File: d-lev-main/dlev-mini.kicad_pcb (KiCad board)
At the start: 4 copper layers, 175.3 x 163.3 mm, 114 parts, among them J1 Conn_01x12_MountingPin, J2 Tag-Connect TC2030-NL, J3 S8B-PH-SM4-TB, J4 S8B-PH-SM4-TB, J5 Conn_01x06_MountingPin, Q1 BSS138, Q3 BSS138, Q4 BSS138, Q5 BSS138, SW1 RotaryEncoder_Switch, SW2 RotaryEncoder_Switch, SW3 RotaryEncoder_Switch, SW4 RotaryEncoder_Switch, SW5 RotaryEncoder_Switch, SW6 RotaryEncoder_Switch, SW7 RotaryEncoder_Switch, SW8 RotaryEncoder_Switch, U1 25LCxxx, U2 AMS1117-3.3, U3 AC608

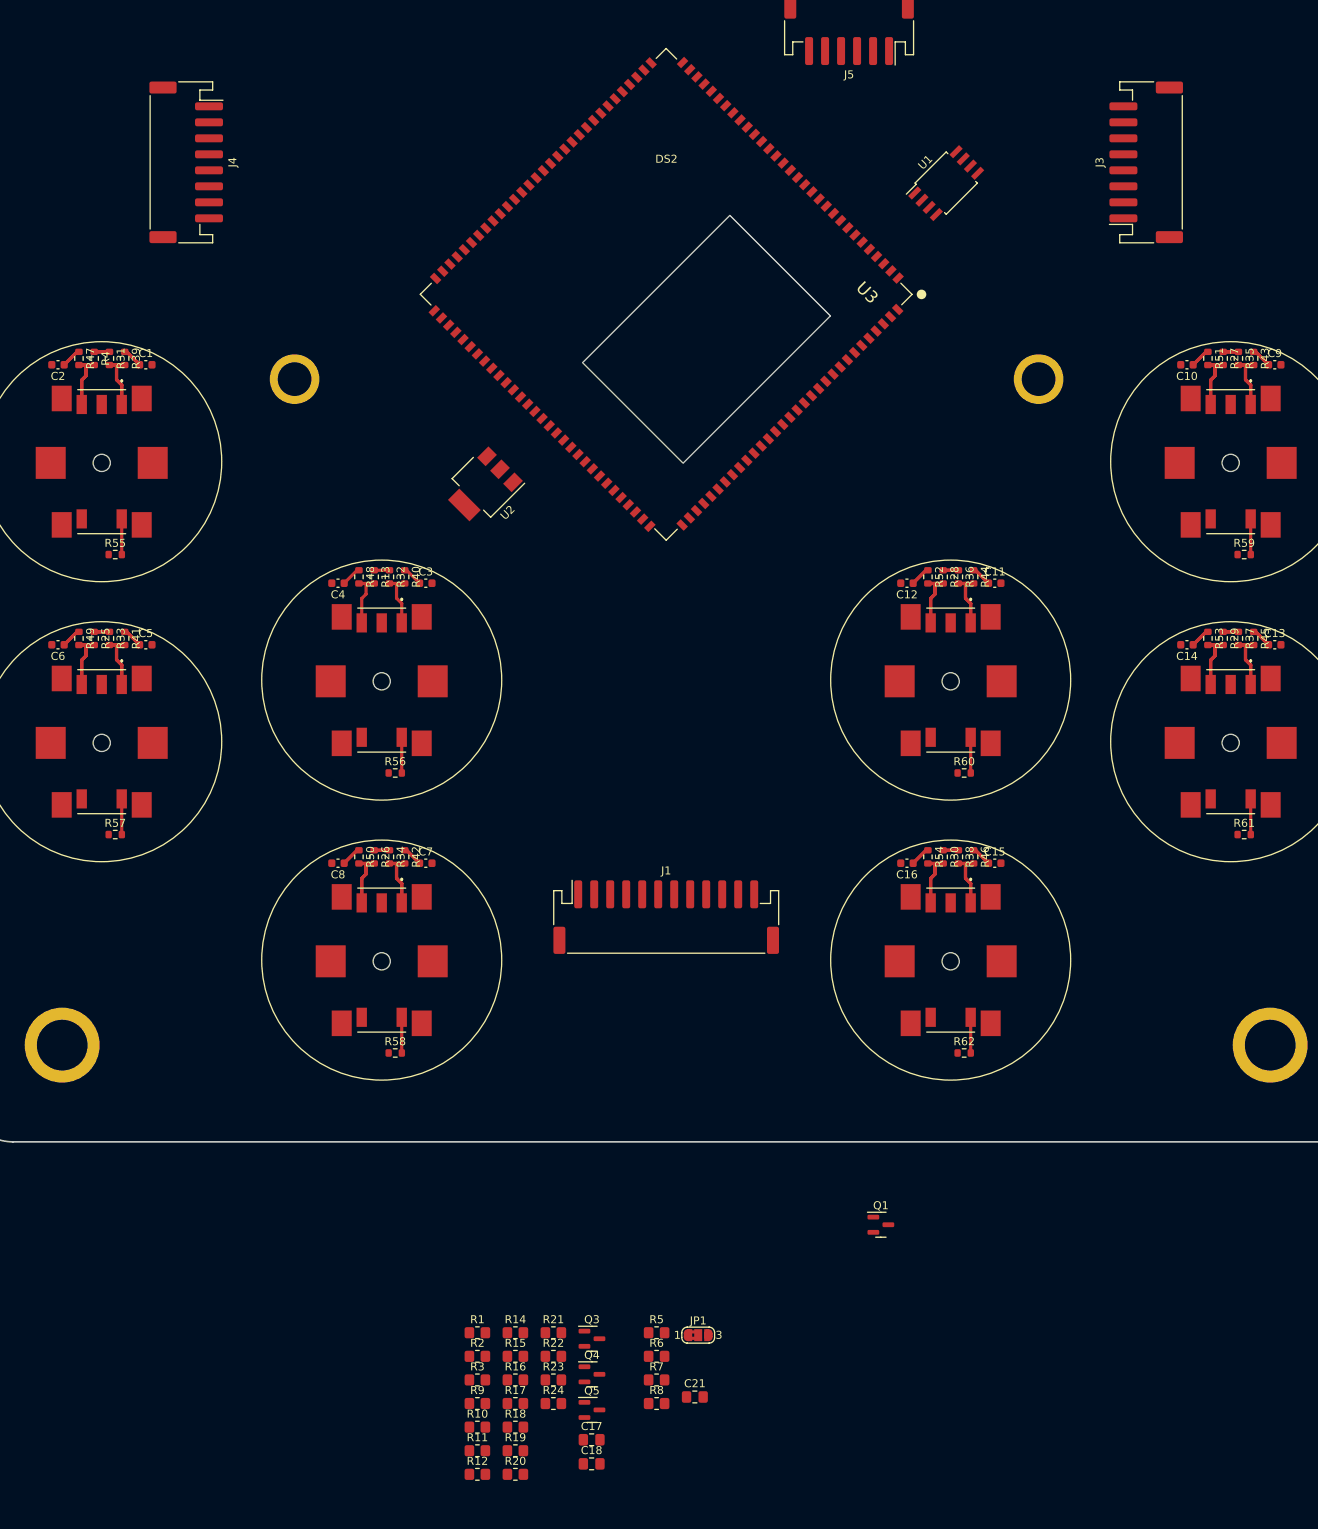
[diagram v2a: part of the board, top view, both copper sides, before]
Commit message: Pinned out FPGA and rearranged encoders again
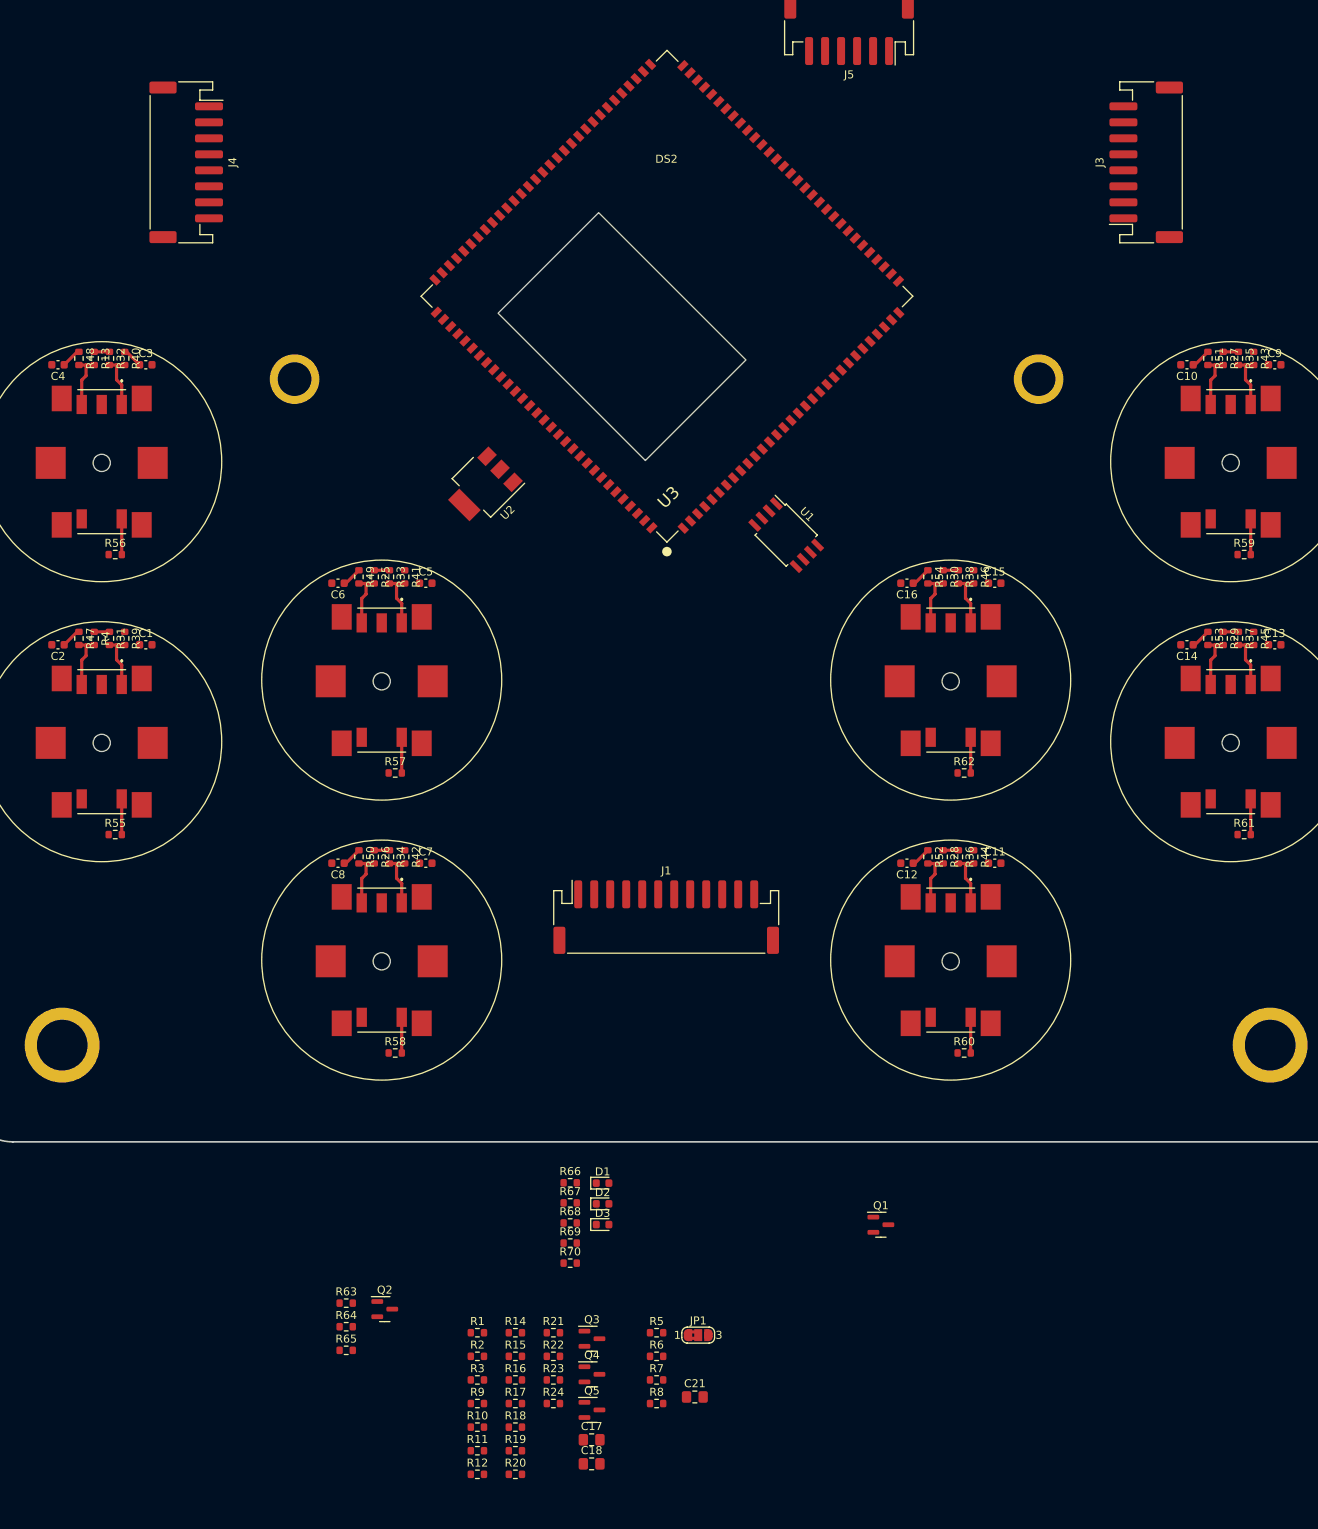
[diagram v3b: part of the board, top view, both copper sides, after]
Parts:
- added D1: LED, LED_SMD:LED_0603_1608Metric, F.Cu at (-7.95, 58.0)
- added D2: LED, LED_SMD:LED_0603_1608Metric, F.Cu at (-7.95, 60.6)
- added D3: LED, LED_SMD:LED_0603_1608Metric, F.Cu at (-7.95, 63.2)
- added Q2: BSS138, Package_TO_SOT_SMD:SOT-23, F.Cu at (-35.2, 73.8)
- added R63: 10k, Resistor_SMD:R_0603_1608Metric, F.Cu at (-40.0, 73.0)
- added R64: 10k, Resistor_SMD:R_0603_1608Metric, F.Cu at (-40.0, 76.0)
- added R65: 220, Resistor_SMD:R_0603_1608Metric, F.Cu at (-40.0, 78.9)
- added R66: 1k, Resistor_SMD:R_0603_1608Metric, F.Cu at (-12.0, 58.0)
- added R67: 1k, Resistor_SMD:R_0603_1608Metric, F.Cu at (-12.0, 60.5)
- added R68: 1k, Resistor_SMD:R_0603_1608Metric, F.Cu at (-12.0, 63.0)
- added R69: 10k, Resistor_SMD:R_0603_1608Metric, F.Cu at (-12.0, 65.5)
- added R70: 10k, Resistor_SMD:R_0603_1608Metric, F.Cu at (-12.0, 68.0)
- R1, R10, R11, R12, R14, R15, R16, R17, R18, R19, R2, R20, R21, R22, R23, R24, R3, R5, R6, R7, R8, R9: footprint Resistor_SMD:R_0805_2012Metric_Pad1.20x1.40mm_HandSolder -> Resistor_SMD:R_0603_1608Metric
- R13, R25, R26, R27, R28, R29, R30, R31, R32, R33, R34, R35, R36, R37, R38, R39, R4, R40, R41, R42, R43, R44, R45, R46, R47, R48, R49, R50, R51, R52, R53, R54, R55, R56, R57, R58, R59, R60, R61, R62: value R_Small -> 10k
- moved U1 48.3 mm to (15.0, -23.0), turned to -45 degrees
- moved C4 44.4 mm to (-76.0, -44.3)
- moved R13 44.4 mm to (-71.5, -45.1)
- moved R32 44.4 mm to (-69.6, -45.1)
- moved R48 44.4 mm to (-73.4, -45.1)
- moved R56 44.4 mm to (-68.9, -20.6)
- moved C3 44.4 mm to (-65.1, -44.3)
- moved R40 44.4 mm to (-67.7, -45.1)
- moved U3 43.2 mm to (-30.6, -52.9), turned to -45 degrees
- moved C6 35.8 mm to (-41.0, -17.0)
- moved R25 35.8 mm to (-36.5, -17.8)
- moved R33 35.8 mm to (-34.6, -17.8)
- moved R49 35.8 mm to (-38.4, -17.8)
- moved R57 35.8 mm to (-33.9, 6.73)
- moved C5 35.8 mm to (-30.1, -17.0)
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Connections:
- C1 pad 1: enc_2.a -> /FPGA/enc_2.b
- C10 pad 1: enc_6.b -> /FPGA/enc_5.a
- C11 pad 1: enc_5.a -> /FPGA/enc_8.b
- C12 pad 1: enc_5.b -> /FPGA/enc_8.a
- C13 pad 1: enc_7.a -> /FPGA/enc_6.b
- C14 pad 1: enc_7.b -> /FPGA/enc_6.a
- C15 pad 1: enc_8.a -> /FPGA/enc_7.b
- C16 pad 1: enc_8.b -> /FPGA/enc_7.a
- C2 pad 1: enc_2.b -> /FPGA/enc_2.a
- C3 pad 1: enc_1.a -> /FPGA/enc_1.b
- C4 pad 1: enc_1.b -> /FPGA/enc_1.a
- C5 pad 1: enc_3.a -> /FPGA/enc_3.b
- C6 pad 1: enc_3.b -> /FPGA/enc_3.a
- C7 pad 1: enc_4.a -> /FPGA/enc_4.b
- C8 pad 1: enc_4.b -> /FPGA/enc_4.a
- C9 pad 1: enc_6.a -> /FPGA/enc_5.b
- J1 pad 3: uart_tx_5v -> midi_out_lo
- J1 pad 4: uart_rx_5v -> midi_in
- J1 pad 5: midi_out_lo -> uart_tx_5v
- J1 pad 6: midi_in -> uart_rx_5v
- R13 pad 2: /encoder/B1 -> /encoder/A1
- R25 pad 2: /encoder2/B1 -> /encoder2/A1
- R26 pad 2: /encoder3/B1 -> /encoder3/A1
- R27 pad 2: /encoder4/B1 -> /encoder4/A1
- R28 pad 2: /encoder7/B1 -> /encoder7/A1
- R29 pad 2: /encoder5/B1 -> /encoder5/A1
- R30 pad 2: /encoder6/B1 -> /encoder6/A1
- R31 pad 2: /encoder1/A1 -> /encoder1/B1
- R32 pad 2: /encoder/A1 -> /encoder/B1
- R33 pad 2: /encoder2/A1 -> /encoder2/B1
- R34 pad 2: /encoder3/A1 -> /encoder3/B1
- R35 pad 2: /encoder4/A1 -> /encoder4/B1
- R36 pad 2: /encoder7/A1 -> /encoder7/B1
- R37 pad 2: /encoder5/A1 -> /encoder5/B1
- R38 pad 2: /encoder6/A1 -> /encoder6/B1
- R39 pad 1: enc_2.a -> /FPGA/enc_2.b
- R39 pad 2: /encoder1/A1 -> /encoder1/B1
- R4 pad 2: /encoder1/B1 -> /encoder1/A1
- R40 pad 1: enc_1.a -> /FPGA/enc_1.b
- R40 pad 2: /encoder/A1 -> /encoder/B1
- R41 pad 1: enc_3.a -> /FPGA/enc_3.b
- R41 pad 2: /encoder2/A1 -> /encoder2/B1
- R42 pad 1: enc_4.a -> /FPGA/enc_4.b
- R42 pad 2: /encoder3/A1 -> /encoder3/B1
- R43 pad 1: enc_6.a -> /FPGA/enc_5.b
- R43 pad 2: /encoder4/A1 -> /encoder4/B1
- R44 pad 1: enc_5.a -> /FPGA/enc_8.b
- R44 pad 2: /encoder7/A1 -> /encoder7/B1
- R45 pad 1: enc_7.a -> /FPGA/enc_6.b
- R45 pad 2: /encoder5/A1 -> /encoder5/B1
- R46 pad 1: enc_8.a -> /FPGA/enc_7.b
- R46 pad 2: /encoder6/A1 -> /encoder6/B1
- R47 pad 1: enc_2.b -> /FPGA/enc_2.a
- R47 pad 2: /encoder1/B1 -> /encoder1/A1
- R48 pad 1: enc_1.b -> /FPGA/enc_1.a
- R48 pad 2: /encoder/B1 -> /encoder/A1
- R49 pad 1: enc_3.b -> /FPGA/enc_3.a
- R49 pad 2: /encoder2/B1 -> /encoder2/A1
- R50 pad 1: enc_4.b -> /FPGA/enc_4.a
- R50 pad 2: /encoder3/B1 -> /encoder3/A1
- R51 pad 1: enc_6.b -> /FPGA/enc_5.a
- R51 pad 2: /encoder4/B1 -> /encoder4/A1
- R52 pad 1: enc_5.b -> /FPGA/enc_8.a
- R52 pad 2: /encoder7/B1 -> /encoder7/A1
- R53 pad 1: enc_7.b -> /FPGA/enc_6.a
- R53 pad 2: /encoder5/B1 -> /encoder5/A1
- R54 pad 1: enc_8.b -> /FPGA/enc_7.a
- R54 pad 2: /encoder6/B1 -> /encoder6/A1
- R55 pad 2: enc_2.s -> /FPGA/enc_2.s
- R56 pad 2: enc_1.s -> /FPGA/enc_1.s
- R57 pad 2: enc_3.s -> /FPGA/enc_3.s
- R58 pad 2: enc_4.s -> /FPGA/enc_4.s
- R59 pad 2: enc_6.s -> /FPGA/enc_5.s
- R60 pad 2: enc_5.s -> /FPGA/enc_8.s
- R61 pad 2: enc_7.s -> /FPGA/enc_6.s
- R62 pad 2: enc_8.s -> /FPGA/enc_7.s
- SW1 pad S1: enc_2.s -> /FPGA/enc_2.s
- SW2 pad S1: enc_1.s -> /FPGA/enc_1.s
- SW3 pad S1: enc_3.s -> /FPGA/enc_3.s
- SW4 pad S1: enc_4.s -> /FPGA/enc_4.s
- SW5 pad S1: enc_6.s -> /FPGA/enc_5.s
- SW6 pad S1: enc_5.s -> /FPGA/enc_8.s
- SW7 pad S1: enc_7.s -> /FPGA/enc_6.s
- SW8 pad S1: enc_8.s -> /FPGA/enc_7.s
- U3 pad 1: unconnected-(U3-IO_T14-Pad1) -> /spdif_tx_0
- U3 pad 10: unconnected-(U3-IO_L15-Pad10) -> /FPGA/mem_spi.di
- U3 pad 100: unconnected-(U3-IO_R3-Pad100) -> /FPGA/enc_3.a
- U3 pad 101: unconnected-(U3-IO_T3-Pad101) -> /FPGA/enc_3.b
- U3 pad 102: unconnected-(U3-IO_R4-Pad102) -> /FPGA/enc_3.s
- U3 pad 103: unconnected-(U3-IO_T4-Pad103) -> /FPGA/enc_4.a
- U3 pad 104: unconnected-(U3-IO_R5-Pad104) -> /FPGA/enc_4.b
- U3 pad 105: unconnected-(U3-IO_T5-Pad105) -> /FPGA/enc_4.s
- U3 pad 11: unconnected-(U3-IO_L16-Pad11) -> /FPGA/mem_spi.cl
- U3 pad 12: unconnected-(U3-IO_P11-Pad12) -> /FPGA/mem_spi.do
- U3 pad 120: unconnected-(U3-IO_R12-Pad120) -> /FPGA/midi_tx_n
- U3 pad 121: unconnected-(U3-IO_T12-Pad121) -> /FPGA/midi_tx
- U3 pad 122: unconnected-(U3-IO_R13-Pad122) -> /FPGA/midi_rx
- U3 pad 123: unconnected-(U3-IO_T13-Pad123) -> /uart_tx_3v
- U3 pad 124: unconnected-(U3-IO_R14-Pad124) -> /uart_rx_3v
- U3 pad 13: unconnected-(U3-IO_N11-Pad13) -> /FPGA/mem_spi.cs
- U3 pad 2: unconnected-(U3-IO_T15-Pad2) -> /spdif_tx_1
- U3 pad 20: unconnected-(U3-IO_K16-Pad20) -> /FPGA/enc_8.s
- U3 pad 21: unconnected-(U3-IO_J15-Pad21) -> /FPGA/enc_8.b
- U3 pad 22: unconnected-(U3-IO_J16-Pad22) -> /FPGA/enc_8.a
- U3 pad 23: unconnected-(U3-IO_L14-Pad23) -> /FPGA/enc_7.s
- U3 pad 24: unconnected-(U3-IO_J14-Pad24) -> /FPGA/enc_7.b
- U3 pad 25: unconnected-(U3-IO_K15-Pad25) -> /FPGA/enc_7.a
- U3 pad 26: unconnected-(U3-IO_F16-Pad26) -> /FPGA/enc_6.s
- U3 pad 27: unconnected-(U3-IO_G15-Pad27) -> /FPGA/enc_6.b
- U3 pad 28: unconnected-(U3-IO_F15-Pad28) -> /FPGA/enc_6.a
- U3 pad 29: unconnected-(U3-I_E16-Pad29) -> /FPGA/enc_5.s
- U3 pad 3: unconnected-(U3-IO_R16-Pad3) -> acal_btn
- U3 pad 30: unconnected-(U3-IO_D16-Pad30) -> /FPGA/enc_5.b
- U3 pad 31: unconnected-(U3-IO_D15-Pad31) -> /FPGA/enc_5.a
- U3 pad 4: unconnected-(U3-IO_P15-Pad4) -> mute_btn
- U3 pad 42: unconnected-(U3-I_A9-Pad42) -> /FPGA/vol.quad
- U3 pad 44: unconnected-(U3-IO_C9-Pad44) -> /FPGA/vol.sq
- U3 pad 46: unconnected-(U3-IO_D9-Pad46) -> /FPGA/vol.zero
- U3 pad 5: unconnected-(U3-IO_P16-Pad5) -> mute_led
- U3 pad 50: unconnected-(U3-I_E1-Pad50) -> /FPGA/~{reset}
- U3 pad 53: unconnected-(U3-IO_D1-Pad53) -> /FPGA/tuner.oe
- U3 pad 54: unconnected-(U3-IO_F3-Pad54) -> /FPGA/tuner.le
- U3 pad 55: unconnected-(U3-IO_F2-Pad55) -> /FPGA/tuner.sda
- U3 pad 56: unconnected-(U3-IO_F1-Pad56) -> /FPGA/tuner.scl
- U3 pad 57: unconnected-(U3-IO_G5-Pad57) -> /FPGA/led1
- U3 pad 58: unconnected-(U3-IO_G2-Pad58) -> /FPGA/led2
- U3 pad 59: unconnected-(U3-IO_G1-Pad59) -> /FPGA/led3
- U3 pad 6: unconnected-(U3-IO_N15-Pad6) -> /FPGA/gpio_o3
- U3 pad 65: unconnected-(U3-IO_K5-Pad65) -> /FPGA/lcd_pwm
- U3 pad 66: unconnected-(U3-IO_L4-Pad66) -> /FPGA/lcd.data3
- U3 pad 67: unconnected-(U3-IO_M6-Pad67) -> /FPGA/lcd.data2
- U3 pad 68: unconnected-(U3-IO_N3-Pad68) -> /FPGA/lcd.data1
- U3 pad 69: unconnected-(U3-IO_N5-Pad69) -> /FPGA/lcd.data0
- U3 pad 7: unconnected-(U3-IO_N16-Pad7) -> /FPGA/gpio_o2
- U3 pad 70: unconnected-(U3-IO_P3-Pad70) -> /FPGA/lcd.e
- U3 pad 71: unconnected-(U3-IO_L7-Pad71) -> /FPGA/lcd.rs
- U3 pad 8: unconnected-(U3-I_M15-Pad8) -> /FPGA/gpio_i3
- U3 pad 86: unconnected-(U3-LVDS_TX1_N-Pad86) -> /FPGA/pitch.quad
- U3 pad 88: unconnected-(U3-LVDS_TX2_N-Pad88) -> /FPGA/pitch.sq
- U3 pad 9: unconnected-(U3-I_M16-Pad9) -> /FPGA/gpio_i2
- U3 pad 90: unconnected-(U3-LVDS_TX3_N-Pad90) -> /FPGA/pitch.zero
- U3 pad 94: unconnected-(U3-LVDS_TX4_N-Pad94) -> /FPGA/enc_1.a
- U3 pad 95: unconnected-(U3-LVDS_TX4_P-Pad95) -> /FPGA/enc_1.b
- U3 pad 96: unconnected-(U3-LVDS_TX5_N-Pad96) -> /FPGA/enc_1.s
- U3 pad 97: unconnected-(U3-LVDS_TX5_P-Pad97) -> /FPGA/enc_2.a
- U3 pad 98: unconnected-(U3-IO_R1-Pad98) -> /FPGA/enc_2.b
- U3 pad 99: unconnected-(U3-IO_T2-Pad99) -> /FPGA/enc_2.s
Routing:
- net +3V3: track 28.6 -> 15.2 mm
- net /encoder4/A1: track 14.2 -> 7.10 mm
- net /encoder7/A1: track 14.2 -> 7.10 mm
- net /encoder6/A1: track 14.2 -> 7.10 mm
- net /encoder5/A1: track 14.2 -> 7.10 mm
- net /encoder1/A1: track 14.2 -> 7.10 mm
- net /encoder2/A1: track 14.2 -> 7.10 mm
- net /encoder3/A1: track 14.2 -> 7.10 mm
- net /encoder2/B1: track 14.1 -> 7.06 mm
- net /encoder1/B1: track 14.1 -> 7.06 mm
- net /encoder7/B1: track 14.1 -> 7.06 mm
- net /encoder6/B1: track 14.1 -> 7.06 mm
- net /encoder3/B1: track 14.1 -> 7.06 mm
- net /encoder4/B1: track 14.1 -> 7.06 mm
- net /encoder5/B1: track 14.1 -> 7.06 mm
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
